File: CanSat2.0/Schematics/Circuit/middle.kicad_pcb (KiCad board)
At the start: 2 copper layers, 16 parts, among them IC1 ATMEGA2560-A, J1 Conn_02x05_Counter_Clockwise, J2 Main connector, J3 Conn_01x09

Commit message: PCBs
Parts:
- moved C7 205.5 mm to (30.5, 30.0)
- moved C6 205.4 mm to (30.8, 28.5)
- moved C4 205.0 mm to (31.5, 27.1)
- moved C5 204.8 mm to (31.9, 25.6)
- moved IC1 203.2 mm to (31.3, 42.9), turned to 90 degrees
- moved R1 203.2 mm to (32.6, 32.0)
- moved C1 202.8 mm to (33.5, 28.1), turned to 90 degrees
- moved J1 201.5 mm to (35.4, 24.9)
- moved J2 192.9 mm to (41.0, 63.0), turned to 120 degrees
- moved J3 190.9 mm to (43.4, 72.3), turned to 120 degrees
- moved R2 189.9 mm to (44.5, 74.9)
- moved R3 187.0 mm to (47.5, 75.7)
- moved C3 170.0 mm to (64.6, 44.0)
- moved CSTECE1 167.6 mm to (67.4, 40.5)
- moved R4 167.2 mm to (67.4, 44.0), turned to 180 degrees
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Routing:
- net GND: track 0.00 -> 172.0 mm, vias 0 -> 10
- net +5V: track 0.00 -> 110.2 mm, vias 0 -> 4
- net /SDA: track 0.00 -> 70.7 mm, vias 0 -> 3
- net /CO2: track 0.00 -> 70.3 mm, vias 0 -> 7
- net /MISO: track 0.00 -> 67.4 mm, vias 0 -> 6
- net /SCL: track 0.00 -> 62.1 mm, vias 0 -> 5
- net /O3: track 0.00 -> 57.0 mm
- net /RX_GPS: track 0.00 -> 53.8 mm, vias 0 -> 4
- net /TX_GPS: track 0.00 -> 53.2 mm, vias 0 -> 4
- net /RX: track 0.00 -> 48.6 mm, vias 0 -> 3
- net /GSM_KEY: track 0.00 -> 46.3 mm, vias 0 -> 3
- net /FC_PWM_4: track 0.00 -> 41.6 mm, vias 0 -> 2
- net /MOSI: track 0.00 -> 39.5 mm, vias 0 -> 1
- net /SERVO: track 0.00 -> 39.4 mm
- net /TX: track 0.00 -> 37.8 mm, vias 0 -> 3
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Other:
- board outline added: 15 x 25.3 mm

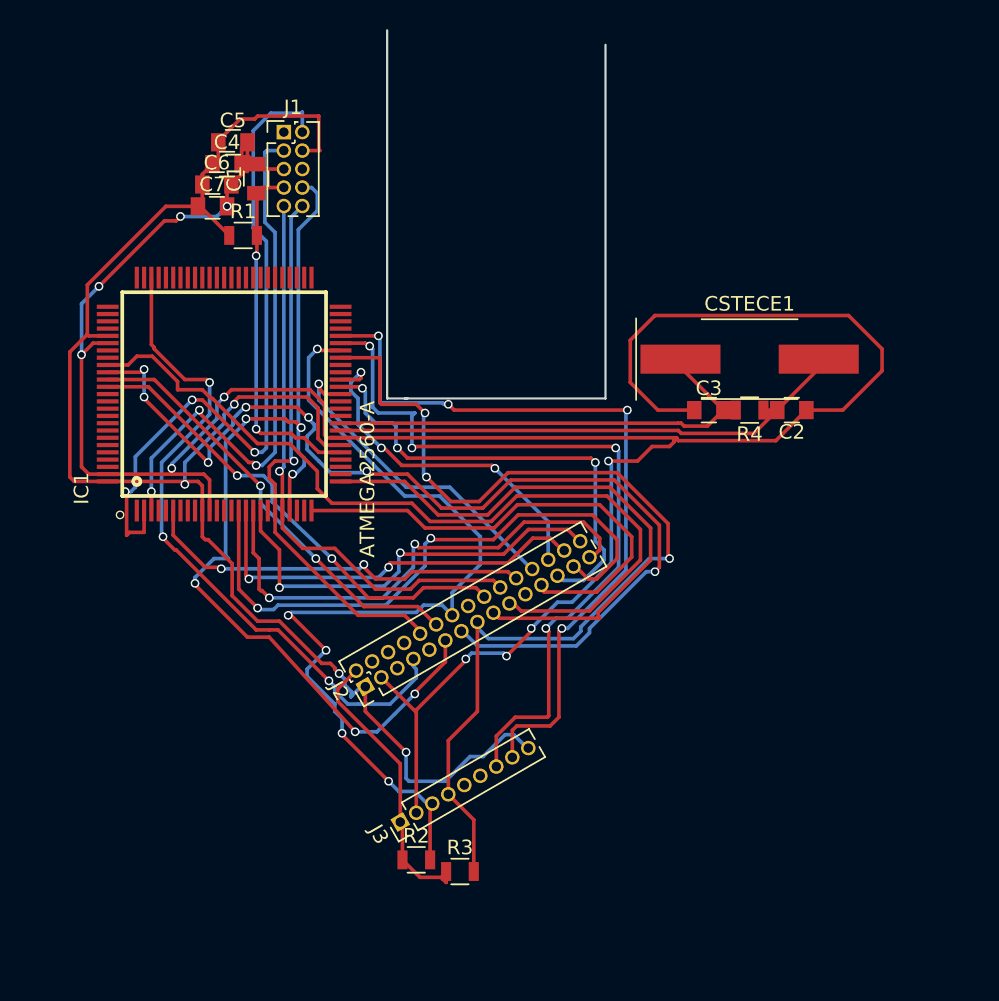
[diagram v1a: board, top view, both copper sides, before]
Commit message: Add three top boards and some other circuitry and modelling
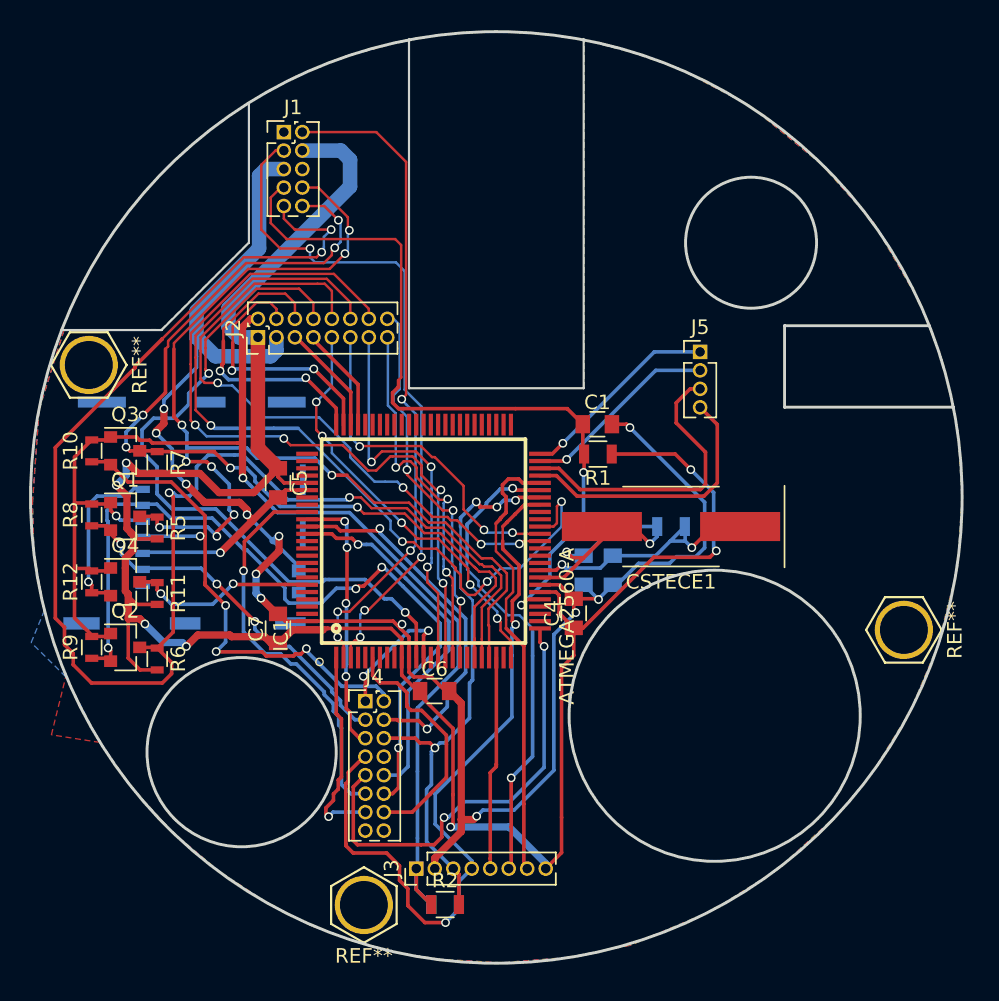
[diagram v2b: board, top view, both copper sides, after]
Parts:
- added J4: Conn_02x07_Counter_Clockwise, Pin_Headers:Pin_Header_Straight_2x08_Pitch1.27mm, F.Cu at (41.0, 64.0)
- added J5: Conn_01x04, Pin_Headers:Pin_Header_Straight_1x04_Pitch1.27mm, F.Cu at (64.0, 40.0)
- added Q1: BSS138, TO_SOT_Packages_SMD:SOT-23, F.Cu at (24.5, 51.3)
- added Q2: BSS138, TO_SOT_Packages_SMD:SOT-23, F.Cu at (24.5, 60.3)
- added Q3: BSS138, TO_SOT_Packages_SMD:SOT-23, F.Cu at (24.5, 46.8)
- added Q4: BSS138, TO_SOT_Packages_SMD:SOT-23, F.Cu at (24.5, 55.8)
- added R10: 10k, Resistors_SMD:R_0603, F.Cu at (22.2, 46.8)
- added R11: 10k, Resistors_SMD:R_0603, F.Cu at (26.7, 56.6)
- added R12: 10k, Resistors_SMD:R_0603, F.Cu at (22.2, 55.8)
- added R5: 10k, Resistors_SMD:R_0603, F.Cu at (26.7, 52.1)
- added R6: 10k, Resistors_SMD:R_0603, F.Cu at (26.7, 61.1)
- added R7: 10k, Resistors_SMD:R_0603, F.Cu at (26.7, 47.6)
- added R8: 10k, Resistors_SMD:R_0603, F.Cu at (22.2, 51.2)
- added R9: 10k, Resistors_SMD:R_0603, F.Cu at (22.2, 60.3)
- added REF**: Standoff, CanSat:Standoff, F.Cu at (40.9, 78.0)
- added REF**: Standoff, CanSat:Standoff, F.Cu at (78.0, 59.1)
- added REF**: Standoff, CanSat:Standoff, F.Cu at (22.0, 40.9)
- added U1: SD, CanSat:SD, B.Cu at (21.0, 43.1)
- C2, C3, R3, R4: moved to B.Cu
- J2: value Main connector -> Conn_02x08_Counter_Clockwise; footprint Pin_Headers:Pin_Header_Straight_2x15_Pitch1.27mm -> Pin_Headers:Pin_Header_Straight_2x08_Pitch1.27mm
- J3: value Conn_01x09 -> Conn_01x08; footprint Pin_Headers:Pin_Header_Straight_1x09_Pitch1.27mm -> Pin_Headers:Pin_Header_Straight_1x08_Pitch1.27mm
- moved C4 39.0 mm to (55.3, 58.0), turned to 90 degrees
- moved C6 37.9 mm to (45.8, 63.3)
- moved C7 29.3 mm to (35.0, 59.0), turned to 90 degrees
- moved C1 28.9 mm to (56.9, 45.0), turned to 0 degrees
- moved R1 28.6 mm to (57.0, 47.0), turned to 180 degrees
- moved J2 25.1 mm to (33.6, 39.0), turned to 90 degrees
- moved C5 23.6 mm to (35.0, 49.0), turned to 270 degrees
- moved C2 18.0 mm to (56.0, 55.0), turned to 90 degrees
- moved IC1 17.0 mm to (45.0, 53.0)
- moved C3 12.8 mm to (58.0, 55.0), turned to 90 degrees
- moved CSTECE1 12.7 mm to (62.0, 52.0), turned to 180 degrees
- moved R4 9.65 mm to (62.0, 52.0), turned to 0 degrees
- moved R2 3.65 mm to (46.5, 78.0)
- moved J3 3.38 mm to (44.5, 75.5), turned to 90 degrees
- moved R3 2.49 mm to (46.5, 78.0)
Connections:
- IC1 pad 1: (no net) -> /RFM_SS
- IC1 pad 12: (no net) -> /GSM_TX
- IC1 pad 13: (no net) -> /GSM_RX
- IC1 pad 23: (no net) -> /SER_P
- IC1 pad 47: (no net) -> /LED4
- IC1 pad 48: (no net) -> /LED3
- IC1 pad 49: (no net) -> /LED2
- IC1 pad 50: (no net) -> /LED1
- IC1 pad 72: (no net) -> /GSM_KEY
- IC1 pad 73: /GSM_KEY -> /FC_EN
- IC1 pad 74: (no net) -> /CAM_EN
- IC1 pad 75: (no net) -> /GSM_SLP
- IC1 pad 94: (no net) -> /SD_SS
- J2 pad 10: /SCK -> /FC_PWM_7
- J2 pad 11: /MISO -> /FC_PWM_6
- J2 pad 12: /O2 -> /FC_PWM_5
- J2 pad 13: /CO2 -> /FC_PWM_4
- J2 pad 14: /SCL -> /FC_PWM_3
- J2 pad 15: /SDA -> /FC_PWM_2
- J2 pad 16: (no net) -> /FC_PWM_1
- J2 pad 4: (no net) -> /CAM_EN
- J2 pad 5: (no net) -> /FC_EN
- J2 pad 6: (no net) -> /GSM_SLP
- J2 pad 8: (no net) -> /GSM_TX
- J2 pad 9: (no net) -> /FC_PWM_8
- J3 pad 5: (no net) -> /SER_P
- J3 pad 6: (no net) -> /RX_GPS
- J3 pad 7: /RX_GPS -> /TX_GPS
- J3 pad 8: /TX_GPS -> +5V
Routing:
- net +3V3: track 19.8 -> 89.4 mm, vias 0 -> 2
- net /MOSI: track 39.5 -> 102.5 mm, vias 1 -> 4
- net /MOSILOW: track 0.00 -> 54.5 mm, vias 0 -> 4
- net /CO2: track 70.3 -> 18.5 mm, vias 7 -> 4
- net /GSM_TX: track 0.00 -> 48.2 mm, vias 0 -> 2
- net +5V: track 110.2 -> 156.1 mm, vias 4 -> 7
- net /GSM_KEY: track 46.3 -> 7.27 mm, vias 3 -> 0
- net /SCKLOW: track 0.00 -> 37.5 mm, vias 0 -> 4
- net /FC_PWM_5: track 24.4 -> 57.1 mm, vias 3 -> 4
- net GND: track 172.0 -> 141.0 mm, vias 10 -> 13
- net /O3: track 57.0 -> 27.4 mm, vias 0 -> 1
- net /RST: track 24.8 -> 53.0 mm
- net /SCK: track 37.6 -> 63.2 mm, vias 1 -> 6
- net /FC_PWM_3: track 28.2 -> 53.8 mm, vias 2 -> 4
- net /MISOLOW: track 0.00 -> 25.5 mm, vias 0 -> 3
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- added copper zone on F.Cu, net +5V
- added copper zone on B.Cu, net GND
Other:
- board size 15 x 25.3 mm -> 64 x 64 mm
- net class Default: clearance 0.2 -> 0.17; trace_width 0.25 -> 0.17
- rule trace_clearance: 0.2 -> 0.17
- rule trace_min: 0.2 -> 0.165

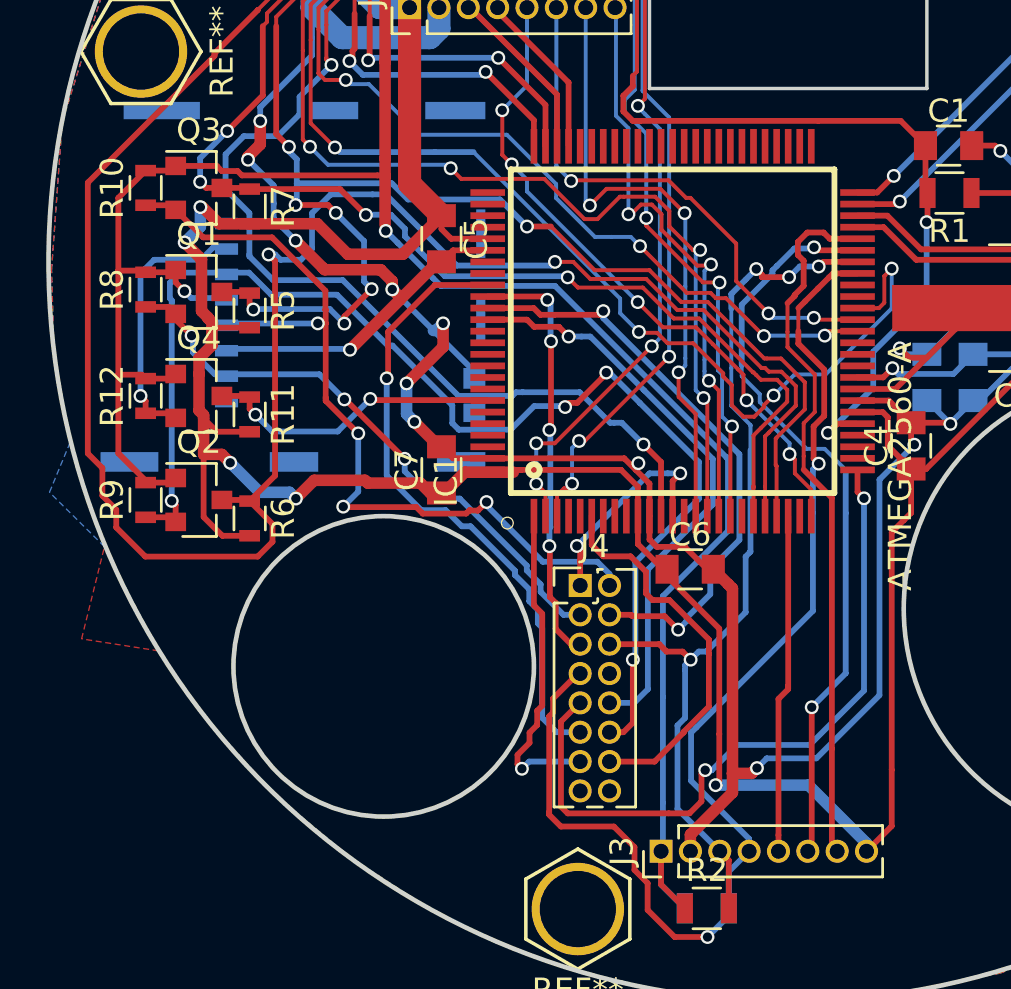
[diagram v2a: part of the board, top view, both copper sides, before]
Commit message: Add new pcbs - center and bottom - and fill the lower half of the model
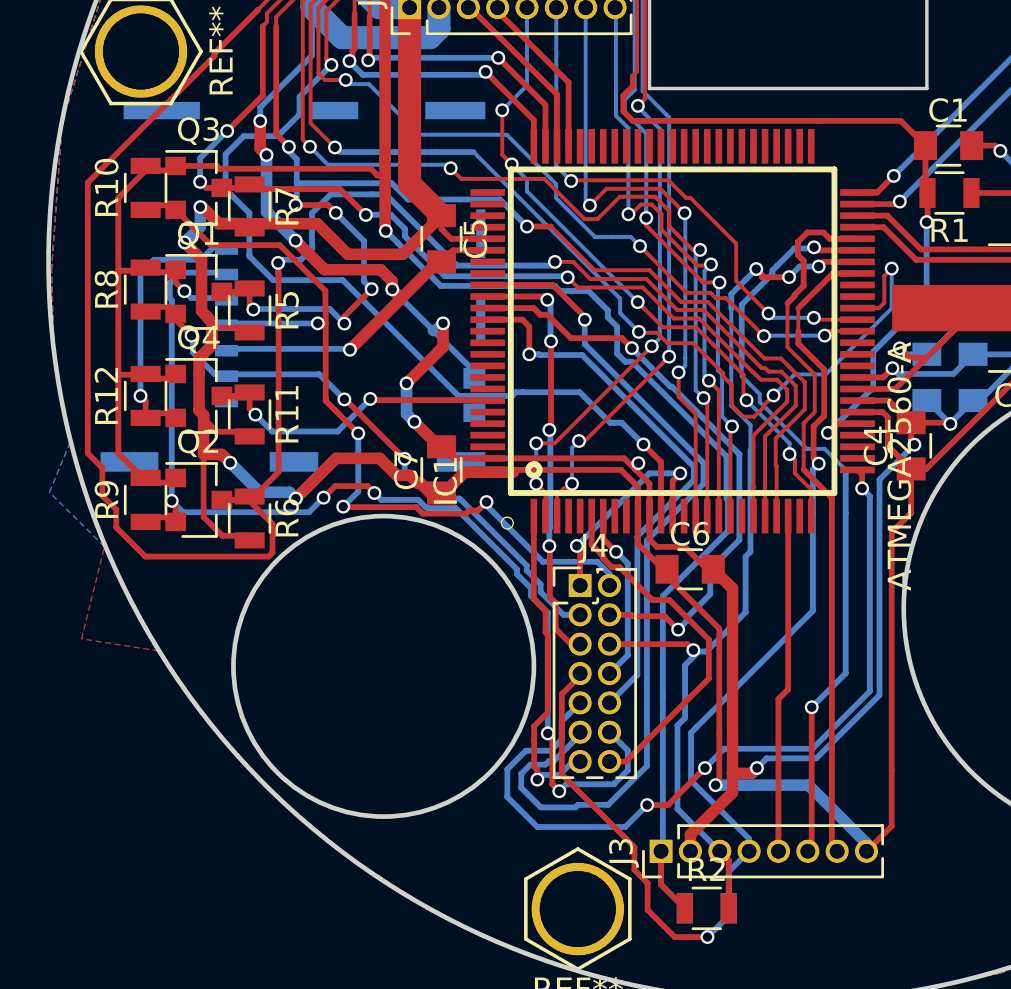
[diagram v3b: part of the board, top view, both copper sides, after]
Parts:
- J4: footprint Pin_Headers:Pin_Header_Straight_2x08_Pitch1.27mm -> Pin_Headers:Pin_Header_Straight_2x07_Pitch1.27mm
- R10, R11, R12, R5, R6, R7, R8, R9: footprint Resistors_SMD:R_0603 -> Resistors_SMD:R_0805
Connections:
- IC1 pad 7: (no net) -> /GAMMA
- J4 pad 8: (no net) -> /GAMMA
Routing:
- net /O3: track 27.4 -> 37.8 mm
- net /GAMMA: track 0.00 -> 7.58 mm, vias 0 -> 1
- net /MOSILOW: track 54.5 -> 47.4 mm, vias 4 -> 5
- net /SERVO: track 30.6 -> 34.5 mm, vias 2 -> 3
- net /SDA: track 52.3 -> 50.4 mm
- net /V_READ: track 25.3 -> 24.0 mm
- net /RFM_INT: track 16.8 -> 15.5 mm
- net GND: track 141.0 -> 141.9 mm
- net +5V: track 156.1 -> 156.9 mm
- net +3V3: track 89.4 -> 90.2 mm
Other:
- net class Default: clearance 0.17 -> 0.165
- rule trace_clearance: 0.17 -> 0.165

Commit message: Middle-conectors
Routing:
- net /MOSI: track 102.3 -> 73.3 mm, vias 4 -> 7
- net /FC_PWM_6: track 23.6 -> 52.0 mm, vias 3 -> 1
- net /GSM_TX: track 48.2 -> 22.8 mm, vias 2 -> 1
- net /CO2: track 18.5 -> 43.0 mm
- net /O2: track 25.4 -> 48.4 mm, vias 2 -> 6
- net /GSM_RX: track 9.53 -> 26.2 mm
- net /FC_PWM_5: track 57.1 -> 40.9 mm, vias 4 -> 2
- net /FC_PWM_4: track 27.0 -> 42.3 mm, vias 3 -> 1
- net /GSM_SLP: track 20.5 -> 6.40 mm, vias 2 -> 0
- net /RST: track 53.0 -> 66.9 mm, vias 2 -> 3
- net /FC_PWM_3: track 53.8 -> 40.5 mm, vias 4 -> 1
- net /FC_PWM_2: track 25.7 -> 38.9 mm, vias 3 -> 1
- net /O3: track 37.8 -> 25.1 mm, vias 1 -> 3
- net /SERVO: track 34.5 -> 22.2 mm, vias 3 -> 1
- net /RFM_INT: track 15.5 -> 3.32 mm
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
